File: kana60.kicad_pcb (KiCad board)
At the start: 2 copper layers, 285.5 x 115.6 mm, 151 parts, among them SW1 SW_PUSH, SW10 SW_PUSH, SW11 SW_PUSH, SW12 SW_PUSH, SW13 SW_PUSH, SW14 SW_PUSH, SW15 SW_PUSH, SW16 SW_PUSH, SW17 SW_PUSH, SW18 SW_PUSH, SW19 SW_PUSH, SW2 SW_PUSH, SW20 SW_PUSH, SW21 SW_PUSH, SW22 SW_PUSH, SW23 SW_PUSH, SW24 SW_PUSH, SW25 SW_PUSH, SW26 SW_PUSH, SW27 SW_PUSH, SW28 SW_PUSH, SW29 SW_PUSH, SW3 SW_PUSH, SW30 SW_PUSH, SW31 SW_PUSH, SW32 SW_PUSH, SW33 SW_PUSH, SW34 SW_PUSH, SW35 SW_PUSH, SW36 SW_PUSH, SW37 SW_PUSH, SW38 SW_PUSH, SW39 SW_PUSH, SW4 SW_PUSH, SW40 SW_PUSH, SW41 SW_PUSH, SW42 SW_PUSH, SW43 SW_PUSH, SW44 SW_PUSH, SW45 SW_PUSH, SW46 SW_PUSH, SW47 SW_PUSH, SW48 SW_PUSH, SW49 SW_PUSH, SW5 SW_PUSH, SW50 SW_PUSH, SW51 SW_PUSH, SW52 SW_PUSH, SW53 SW_PUSH, SW54 SW_PUSH, SW55 SW_PUSH, SW56 SW_PUSH, SW57 SW_PUSH, SW58 SW_PUSH, SW59 SW_PUSH, SW6 SW_PUSH, SW60 SW_PUSH, SW61 SW_PUSH, SW62 SW_PUSH, SW63 SW_PUSH, SW64 SW_PUSH, SW65 SW_PUSH, SW66 SW_PUSH, SW67 SW_PUSH, SW68 SW_PUSH, SW69 SW_PUSH, SW7 SW_PUSH, SW70 SW_PUSH, SW71 SW_Push, SW8 SW_PUSH, SW9 SW_PUSH, U1 ProMicro

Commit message: add GND plane
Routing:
- added copper zone on B.Cu, net GND
- added copper zone on F.Cu, net GND
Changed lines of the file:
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@@
   (segment (start 99.371685 115.062) (end 98.044 115.062) (width 0.25) (layer B.Cu) (net 89))
   (via (at 98.044 115.062) (size 0.8) (drill 0.4) (layers F.Cu B.Cu) (net 89))
+  (segment (start 72.69442 33.3877) (end 72.69442 36.77958) (width 0.25) (layer F.Cu) (net 89))
+  (segment (start 72.413988 37.060012) (end 72.413988 51.839988) (width 0.25) (layer F.Cu) (net 89))
+  (segment (start 72.69442 36.77958) (end 72.413988 37.060012) (width 0.25) (layer F.Cu) (net 89))
+  (segment (start 96.266 99.149712) (end 96.266 114.554) (width 0.25) (layer F.Cu) (net 89))
+  (segment (start 72.413988 51.839988) (end 82.042 61.468) (width 0.25) (layer F.Cu) (net 89))
+  (segment (start 82.042 61.468) (end 82.042 74.765712) (width 0.25) (layer F.Cu) (net 89))
   (segment (start 86.868 89.751712) (end 96.266 99.149712) (width 0.25) (layer F.Cu) (net 89))
+  (segment (start 86.868 79.591712) (end 86.868 89.751712) (width 0.25) (layer F.Cu) (net 89))
+  (segment (start 96.266 114.554) (end 96.774 115.062) (width 0.25) (layer F.Cu) (net 89))
+  (segment (start 96.774 115.062) (end 98.044 115.062) (width 0.25) (layer F.Cu) (net 89))
   (segment (start 82.042 74.765712) (end 86.868 79.591712) (width 0.25) (layer F.Cu) (net 89))
-  (segment (start 96.774 115.062) (end 98.044 115.062) (width 0.25) (layer F.Cu) (net 89))
-  (segment (start 72.69442 33.3877) (end 72.69442 36.77958) (width 0.25) (layer F.Cu) (net 89))
-  (segment (start 72.413988 51.839988) (end 82.042 61.468) (width 0.25) (layer F.Cu) (net 89))
-  (segment (start 72.413988 37.060012) (end 72.413988 51.839988) (width 0.25) (layer F.Cu) (net 89))
-  (segment (start 96.266 99.149712) (end 96.266 114.554) (width 0.25) (layer F.Cu) (net 89))
-  (segment (start 72.69442 36.77958) (end 72.413988 37.060012) (width 0.25) (layer F.Cu) (net 89))
-  (segment (start 96.266 114.554) (end 96.774 115.062) (width 0.25) (layer F.Cu) (net 89))
-  (segment (start 86.868 79.591712) (end 86.868 89.751712) (width 0.25) (layer F.Cu) (net 89))
-  (segment (start 82.042 61.468) (end 82.042 74.765712) (width 0.25) (layer F.Cu) (net 89))
+  (zone (net 79) (net_name GND) (layer B.Cu) (hatch edge 0.508)
+    (connect_pads (clearance 0.508))
+    (min_thickness 0.254)
+    (fill yes (arc_segments 32) (thermal_gap 0.508) (thermal_bridge_width 0.508))
+    (polygon
+      (pts
+        (xy 16.025988 19.2907) (xy 37.107988 19.2907) (xy 301.521988 19.2907) (xy 301.521988 134.8607) (xy 16.025988 134.8607)
+      )
+    )
+  )
+  (zone (net 79) (net_name GND) (layer F.Cu) (hatch edge 0.508)
+    (connect_pads (clearance 0.508))
+    (min_thickness 0.254)
+    (fill yes (arc_segments 32) (thermal_gap 0.508) (thermal_bridge_width 0.508))
+    (polygon
+      (pts
+        (xy 16.025988 19.2907) (xy 71.905988 19.2907) (xy 301.521988 19.2907) (xy 301.521988 134.8607) (xy 16.025988 134.8607)
+      )
+    )
+  )
 )

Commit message: trim anntena
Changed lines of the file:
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@@
   (segment (start 96.774 115.062) (end 98.044 115.062) (width 0.25) (layer F.Cu) (net 89))
   (segment (start 82.042 74.765712) (end 86.868 79.591712) (width 0.25) (layer F.Cu) (net 89))
+  (zone (net 79) (net_name GND) (layer F.Cu) (hatch edge 0.508)
+    (connect_pads (clearance 0.508))
+    (min_thickness 0.254)
+    (fill yes (arc_segments 32) (thermal_gap 0.508) (thermal_bridge_width 0.508))
+    (polygon
+      (pts
+        (xy 301.521988 134.8607) (xy 16.025988 134.8607) (xy 16.025988 19.2907) (xy 301.521988 19.2907)
+      )
+    )
+    (polygon
+      (pts
+        (xy 126.388988 98.9197) (xy 127.150988 99.6817) (xy 128.420988 99.6817) (xy 129.182988 100.1897) (xy 129.563988 100.8247)
+        (xy 131.087988 100.8247) (xy 129.182988 98.9197)
+      )
+    )
+    (polygon
+      (pts
+        (xy 129.690988 98.2847) (xy 131.214988 99.9357) (xy 135.405988 99.9357) (xy 135.405988 98.2847)
+      )
+    )
+    (polygon
+      (pts
+        (xy 67.460988 92.6967) (xy 72.286988 97.6497) (xy 73.302988 98.1577) (xy 73.937988 97.5227) (xy 73.556988 96.7607)
+        (xy 67.460988 90.9187)
+      )
+    )
+    (polygon
+      (pts
+        (xy 68.857988 90.7917) (xy 74.445988 96.3797) (xy 74.953988 96.6337) (xy 75.588988 96.1257) (xy 68.857988 89.6487)
+      )
+    )
+    (polygon
+      (pts
+        (xy 113.561988 81.0127) (xy 116.228988 81.0127) (xy 113.561988 78.4727)
+      )
+    )
+    (polygon
+      (pts
+        (xy 140.485988 77.3297) (xy 140.485988 78.7267) (xy 142.771988 78.7267) (xy 142.771988 77.5837) (xy 141.120988 77.5837)
+        (xy 141.120988 77.3297)
+      )
+    )
+    (polygon
+      (pts
+        (xy 37.996988 77.8377) (xy 39.520988 76.1867) (xy 37.996988 74.6627)
+      )
+    )
+    (polygon
+      (pts
+        (xy 101.877988 76.6947) (xy 101.877988 77.7107) (xy 107.592988 77.7107) (xy 107.592988 76.6947)
+      )
+    )
+    (polygon
+      (pts
+        (xy 97.940988 77.2027) (xy 100.099988 77.2027) (xy 100.099988 75.0437)
+      )
+    )
+    (polygon
+      (pts
+        (xy 141.501988 75.5517) (xy 141.501988 76.6947) (xy 145.819988 76.6947) (xy 145.819988 75.5517)
+      )
+    )
+    (polygon
+      (pts
+        (xy 102.639988 74.5357) (xy 102.639988 75.6787) (xy 107.719988 75.6787) (xy 107.719988 74.5357)
+      )
+    )
+    (polygon
+      (pts
+        (xy 142.263988 73.5197) (xy 142.263988 74.6627) (xy 148.867988 74.6627) (xy 148.867988 73.5197)
+      )
+    )
+    (polygon
+      (pts
+        (xy 103.401988 72.5037) (xy 103.401988 73.6467) (xy 110.767988 73.6467) (xy 110.767988 72.5037)
+      )
+    )
+    (polygon
+      (pts
+        (xy 97.559988 72.7577) (xy 99.337988 72.7577) (xy 99.337988 70.8527)
+      )
+    )
+    (polygon
+      (pts
+        (xy 59.713988 38.2137) (xy 59.713988 38.5947) (xy 55.649988 42.6587) (xy 55.649988 44.6907) (xy 62.126988 38.2137)
+      )
+    )
+    (polygon
+      (pts
+        (xy 29.487988 39.9917) (xy 33.805988 44.3097) (xy 33.805988 42.2777) (xy 32.027988 40.4997) (xy 32.027988 39.9917)
+      )
+    )
+    (polygon
+      (pts
+        (xy 79.779988 36.6897) (xy 79.779988 37.1977) (xy 74.953988 42.0237) (xy 74.953988 44.0557) (xy 82.319988 36.6897)
+      )
+    )
+    (polygon
+      (pts
+        (xy 39.520988 37.4517) (xy 39.520988 37.9597) (xy 35.964988 41.5157) (xy 35.964988 43.5477) (xy 42.187988 37.4517)
+      )
+    )
+    (polygon
+      (pts
+        (xy 222.146988 41.8967) (xy 222.146988 43.4207) (xy 223.416988 41.8967)
+      )
+    )
+    (polygon
+      (pts
+        (xy 56.284988 38.2137) (xy 56.284988 38.7217) (xy 54.506988 40.4997) (xy 54.506988 42.5317) (xy 58.824988 38.2137)
+      )
+    )
+    (polygon
+      (pts
+        (xy 76.604988 36.6897) (xy 76.604988 37.0707) (xy 73.937988 39.7377) (xy 73.937988 41.6427) (xy 78.890988 36.6897)
+      )
+    )
+    (polygon
+      (pts
+        (xy 32.916988 39.9917) (xy 34.440988 41.5157) (xy 34.440988 39.9917)
+      )
+    )
+    (polygon
+      (pts
+        (xy 121.562988 38.9757) (xy 122.959988 41.5157) (xy 125.372988 38.9757)
+      )
+    )
+    (polygon
+      (pts
+        (xy 36.218988 37.5787) (xy 36.218988 38.8487) (xy 35.329988 39.7377) (xy 35.329988 40.8807) (xy 38.631988 37.5787)
+      )
+    )
+    (polygon
+      (pts
+        (xy 66.444988 36.4357) (xy 70.889988 40.8807) (xy 70.889988 39.1027) (xy 68.857988 37.0707) (xy 68.857988 36.4357)
+      )
+    )
+    (polygon
+      (pts
+        (xy 49.680988 37.9597) (xy 52.220988 40.6267) (xy 52.220988 37.9597)
+      )
+    )
+    (polygon
+      (pts
+        (xy 52.982988 37.9597) (xy 52.982988 38.0867) (xy 53.363988 38.8487) (xy 53.617988 40.2457) (xy 55.522988 38.4677)
+        (xy 55.522988 37.9597)
+      )
+    )
+    (polygon
+      (pts
+        (xy 72.921988 36.8167) (xy 72.921988 39.4837) (xy 75.588988 36.8167)
+      )
+    )
+    (polygon
+      (pts
+        (xy 161.821988 39.1027) (xy 162.710988 39.1027) (xy 162.710988 34.6577) (xy 161.821988 33.6417)
+      )
+    )
+    (polygon
+      (pts
+        (xy 69.619988 36.4357) (xy 72.159988 38.9757) (xy 72.159988 36.4357)
+      )
+    )
+    (polygon
+      (pts
+        (xy 42.822988 36.1817) (xy 42.822988 38.7217) (xy 45.362988 36.1817)
+      )
+    )
+    (polygon
+      (pts
+        (xy 83.208988 34.5307) (xy 83.208988 37.1977) (xy 83.970988 37.1977) (xy 83.970988 33.8957)
+      )
+    )
+    (polygon
+      (pts
+        (xy 46.251988 34.5307) (xy 46.251988 36.6897) (xy 47.013988 36.6897) (xy 47.013988 34.0227)
+      )
+    )
+    (polygon
+      (pts
+        (xy 47.013988 24.3707) (xy 47.013988 28.4347) (xy 48.029988 27.4187) (xy 48.029988 24.3707)
+      )
+    )
+    (polygon
+      (pts
+        (xy 43.711988 25.2597) (xy 43.711988 27.0377) (xy 44.727988 27.0377) (xy 44.727988 24.2437)
+      )
+    )
+  )
   (zone (net 79) (net_name GND) (layer B.Cu) (hatch edge 0.508)
     (connect_pads (clearance 0.508))
@@
     (polygon
       (pts
-        (xy 16.025988 19.2907) (xy 37.107988 19.2907) (xy 301.521988 19.2907) (xy 301.521988 134.8607) (xy 16.025988 134.8607)
-      )
-    )
-  )
-  (zone (net 79) (net_name GND) (layer F.Cu) (hatch edge 0.508)
-    (connect_pads (clearance 0.508))
-    (min_thickness 0.254)
-    (fill yes (arc_segments 32) (thermal_gap 0.508) (thermal_bridge_width 0.508))
-    (polygon
-      (pts
-        (xy 16.025988 19.2907) (xy 71.905988 19.2907) (xy 301.521988 19.2907) (xy 301.521988 134.8607) (xy 16.025988 134.8607)
-      )
-    )
+        (xy 301.521988 134.8607) (xy 16.025988 134.8607) (xy 16.025988 19.2907) (xy 301.521988 19.2907)
+      )
+    )
+    (polygon
+      (pts
+        (xy 109.370988 76.6947) (xy 109.370988 77.7107) (xy 144.295988 77.7107) (xy 144.295988 76.6947)
+      )
+    )

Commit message: change revision to 1.1 from 1.0
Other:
- board text added: "rev.1.1"
- board text removed: "rev.1.0"
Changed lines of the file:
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@@
   (title_block
     (title kana60)
-    (date 2019-07-02)
-    (rev rev.1)
+    (date 2019-10-13)
+    (rev rev.1.1)
     (comment 1 https://github.com/sasaplus1/kana60)
     (comment 2 "designed by sasa+1")
@@
   (gr_line (start 301.521988 133.0827) (end 301.521988 21.0687) (layer Edge.Cuts) (width 0.2))
   (gr_line (start 17.803988 19.2907) (end 299.743988 19.2907) (layer Edge.Cuts) (width 0.2))
-  (gr_text rev.1.0 (at 226.314 76.962) (layer B.SilkS)
+  (gr_text rev.1.1 (at 226.314 76.962) (layer B.SilkS)
     (effects (font (size 1 1) (thickness 0.15)) (justify mirror))
   )

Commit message: update captions
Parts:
- moved G*** 0.75 mm to (243.3, 75.2)
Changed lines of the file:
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@@
   )
   (module kana60:kana60-title (layer B.Cu)
-    (at 243.332 74.422 180)
+    (at 243.332 75.1707 180)
     (fp_text reference G*** (at 0 0) (layer B.SilkS) hide
       (effects (font (size 1.524 1.524) (thickness 0.3)) (justify mirror))
@@
   (gr_line (start 301.521988 133.0827) (end 301.521988 21.0687) (layer Edge.Cuts) (width 0.2))
   (gr_line (start 17.803988 19.2907) (end 299.743988 19.2907) (layer Edge.Cuts) (width 0.2))
-  (gr_text rev.1.1 (at 226.314 76.962) (layer B.SilkS)
-    (effects (font (size 1 1) (thickness 0.15)) (justify mirror))
+  (gr_text rev.1.1 (at 225.067988 77.7107) (layer B.SilkS)
+    (effects (font (size 1.2 1.2) (thickness 0.15)) (justify mirror))
   )
-  (gr_text "designed by sasa+1" (at 78.001988 75.1707) (layer B.SilkS)
-    (effects (font (size 1 1) (thickness 0.15)) (justify mirror))
+  (gr_text "designed by sasa+1" (at 78.001988 76.1867) (layer B.SilkS)
+    (effects (font (size 1.2 1.2) (thickness 0.15)) (justify mirror))
   )
   (gr_line (start 285.11475 56.27635) (end 285.11475 42.27675) (layer Dwgs.User) (width 0.2))

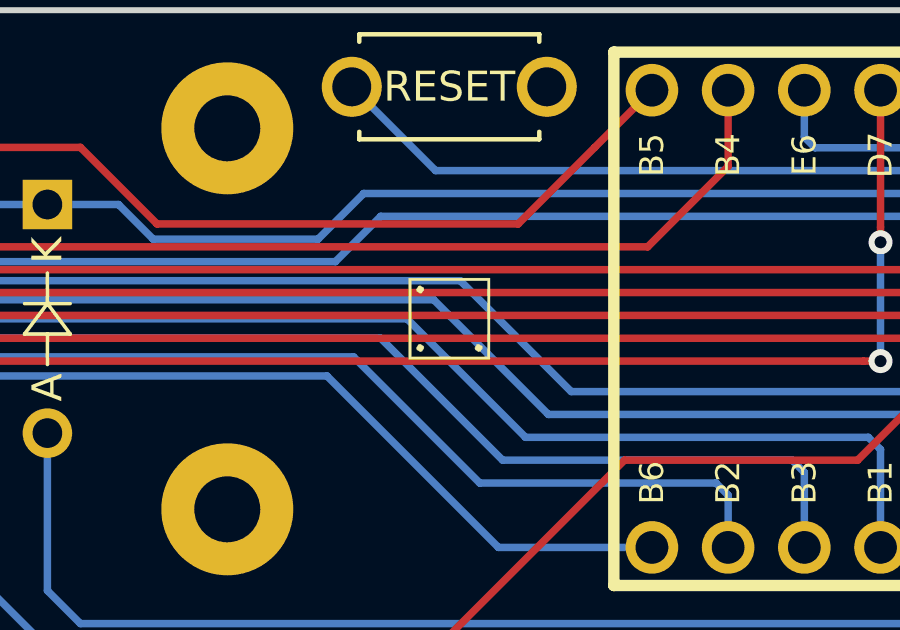
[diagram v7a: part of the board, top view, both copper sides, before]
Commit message: update icon
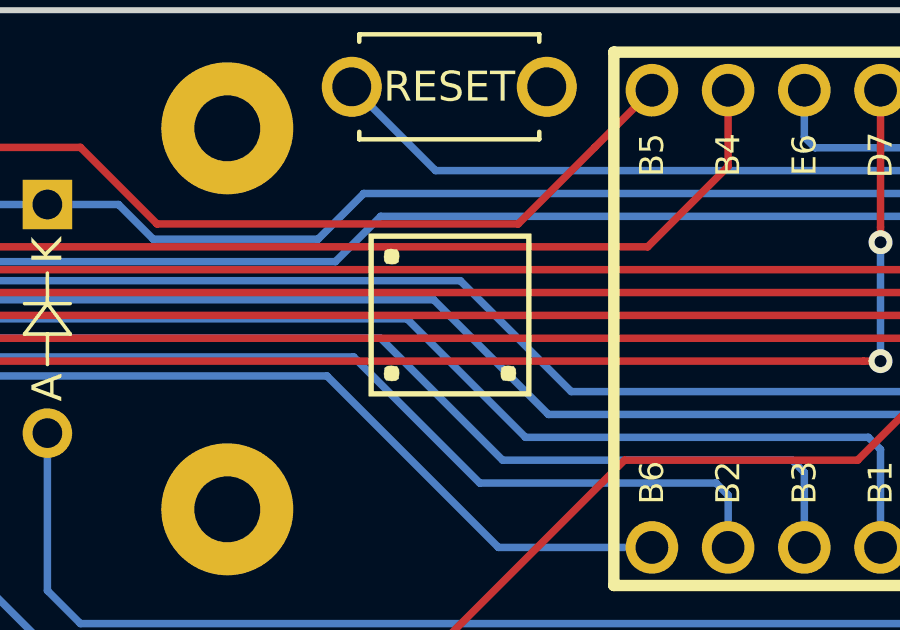
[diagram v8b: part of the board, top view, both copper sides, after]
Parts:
- removed the G*** at (67.6, 75.2)
- removed the G*** at (260.6, 29.6)
- added G***: LOGO, kicad-footprints:sasaplus1-icon-64, F.Cu at (260.6, 29.5)
- added G***: LOGO, kicad-footprints:sasaplus1-icon-48, B.Cu at (64.5, 76.2)
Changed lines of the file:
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@@
     (add_net GND)
+  )
+  (module kicad-footprints:sasaplus1-icon-64 (layer F.Cu)
+    (at 260.627988 29.4507)
+    (fp_text reference G*** (at 0 0) (layer F.SilkS) hide
+      (effects (font (size 1.524 1.524) (thickness 0.3)))
+    )
+    (fp_text value LOGO (at 0 0) (layer F.SilkS) hide
+      (effects (font (size 1.524 1.524) (thickness 0.3)))
+    )
+    (fp_poly (pts (xy -1.767425 -2.180354) (xy -1.701115 -2.081394) (xy -1.693333 -1.947333) (xy -1.714313 -1.767425)
+      (xy -1.813273 -1.701115) (xy -1.947333 -1.693333) (xy -2.127242 -1.714313) (xy -2.193552 -1.813273)
+      (xy -2.201333 -1.947333) (xy -2.180354 -2.127242) (xy -2.081394 -2.193552) (xy -1.947333 -2.201333)
+      (xy -1.767425 -2.180354)) (layer F.SilkS) (width 0.01))
+    (fp_poly (pts (xy 2.127241 1.714312) (xy 2.193552 1.813273) (xy 2.201333 1.947333) (xy 2.180354 2.127241)
+      (xy 2.081393 2.193552) (xy 1.947333 2.201333) (xy 1.767425 2.180354) (xy 1.701115 2.081393)
+      (xy 1.693333 1.947333) (xy 1.714312 1.767425) (xy 1.813273 1.701115) (xy 1.947333 1.693333)
+      (xy 2.127241 1.714312)) (layer F.SilkS) (width 0.01))
+    (fp_poly (pts (xy -1.767425 1.714312) (xy -1.701115 1.813273) (xy -1.693333 1.947333) (xy -1.714313 2.127241)
+      (xy -1.813273 2.193552) (xy -1.947333 2.201333) (xy -2.127242 2.180354) (xy -2.193552 2.081393)
+      (xy -2.201333 1.947333) (xy -2.180354 1.767425) (xy -2.081394 1.701115) (xy -1.947333 1.693333)
+      (xy -1.767425 1.714312)) (layer F.SilkS) (width 0.01))
+    (fp_poly (pts (xy 2.709333 2.709333) (xy -2.709333 2.709333) (xy -2.709333 -2.54) (xy -2.54 -2.54)
+      (xy -2.54 2.54) (xy 2.54 2.54) (xy 2.54 -2.54) (xy -2.54 -2.54)
+      (xy -2.709333 -2.54) (xy -2.709333 -2.709333) (xy 2.709333 -2.709333) (xy 2.709333 2.709333)) (layer F.SilkS) (width 0.01))
+  )
+  (module kicad-footprints:sasaplus1-icon-48 (layer B.Cu)
+    (at 64.539988 76.1867 180)
+    (fp_text reference G*** (at 0 0) (layer B.SilkS) hide
+      (effects (font (size 1.524 1.524) (thickness 0.3)) (justify mirror))
+    )
+    (fp_text value LOGO (at 0 0) (layer B.SilkS) hide
+      (effects (font (size 1.524 1.524) (thickness 0.3)) (justify mirror))
+    )
+    (fp_poly (pts (xy -1.235879 1.573698) (xy -1.186228 1.436007) (xy -1.185334 1.397) (xy -1.220303 1.235879)
+      (xy -1.357994 1.186228) (xy -1.397 1.185334) (xy -1.558122 1.220303) (xy -1.607773 1.357994)
+      (xy -1.608667 1.397) (xy -1.573698 1.558122) (xy -1.436007 1.607773) (xy -1.397 1.608667)
+      (xy -1.235879 1.573698)) (layer B.SilkS) (width 0.01))
+    (fp_poly (pts (xy 1.558121 -1.220302) (xy 1.607772 -1.357993) (xy 1.608666 -1.397) (xy 1.573697 -1.558121)
+      (xy 1.436006 -1.607772) (xy 1.397 -1.608666) (xy 1.235878 -1.573697) (xy 1.186227 -1.436006)
+      (xy 1.185333 -1.397) (xy 1.220302 -1.235878) (xy 1.357993 -1.186227) (xy 1.397 -1.185333)
+      (xy 1.558121 -1.220302)) (layer B.SilkS) (width 0.01))
+    (fp_poly (pts (xy -1.235879 -1.220302) (xy -1.186228 -1.357993) (xy -1.185334 -1.397) (xy -1.220303 -1.558121)
+      (xy -1.357994 -1.607772) (xy -1.397 -1.608666) (xy -1.558122 -1.573697) (xy -1.607773 -1.436006)
+      (xy -1.608667 -1.397) (xy -1.573698 -1.235878) (xy -1.436007 -1.186227) (xy -1.397 -1.185333)
+      (xy -1.235879 -1.220302)) (layer B.SilkS) (width 0.01))
+    (fp_poly (pts (xy 2.032 -2.032) (xy -2.032 -2.032) (xy -2.032 1.862667) (xy -1.862667 1.862667)
+      (xy -1.862667 -1.862666) (xy 1.862666 -1.862666) (xy 1.862666 1.862667) (xy -1.862667 1.862667)
+      (xy -2.032 1.862667) (xy -2.032 2.032) (xy 2.032 2.032) (xy 2.032 -2.032)) (layer B.SilkS) (width 0.01))
   )
   (module Keebio-Parts:Hybrid_PCB_125H (layer F.Cu)
@@
       (xy -7.044052 1.138264)) (layer B.SilkS) (width 0.01))
   )
-  (module kicad-footprints:sasaplus1-icon (layer B.Cu)
-    (at 67.564 75.184 180)
-    (fp_text reference G*** (at 0 0) (layer B.SilkS) hide
-      (effects (font (size 1.524 1.524) (thickness 0.3)) (justify mirror))
-    )
-    (fp_text value LOGO (at 0.75 0) (layer B.SilkS) hide
-      (effects (font (size 1.524 1.524) (thickness 0.3)) (justify mirror))
-    )
-    (fp_poly (pts (xy -0.861418 1.032894) (xy -0.846666 0.973666) (xy -0.914439 0.861418) (xy -0.973666 0.846666)
-      (xy -1.085915 0.914439) (xy -1.100666 0.973666) (xy -1.032894 1.085915) (xy -0.973666 1.100666)
-      (xy -0.861418 1.032894)) (layer B.SilkS) (width 0.01))
-    (fp_poly (pts (xy 1.085915 -0.91444) (xy 1.100667 -0.973667) (xy 1.032894 -1.085915) (xy 0.973667 -1.100667)
-      (xy 0.861418 -1.032894) (xy 0.846667 -0.973667) (xy 0.91444 -0.861418) (xy 0.973667 -0.846667)
-      (xy 1.085915 -0.91444)) (layer B.SilkS) (width 0.01))
-    (fp_poly (pts (xy -0.861418 -0.91444) (xy -0.846666 -0.973667) (xy -0.914439 -1.085915) (xy -0.973666 -1.100667)
-      (xy -1.085915 -1.032894) (xy -1.100666 -0.973667) (xy -1.032894 -0.861418) (xy -0.973666 -0.846667)
-      (xy -0.861418 -0.91444)) (layer B.SilkS) (width 0.01))
-    (fp_poly (pts (xy 1.354667 -1.354667) (xy -1.354666 -1.354667) (xy -1.354666 1.27) (xy -1.27 1.27)
-      (xy -1.27 -1.27) (xy 1.27 -1.27) (xy 1.27 1.27) (xy -1.27 1.27)
-      (xy -1.354666 1.27) (xy -1.354666 1.354666) (xy 1.354667 1.354666) (xy 1.354667 -1.354667)) (layer B.SilkS) (width 0.01))
-  )
-  (module kicad-footprints:sasaplus1-icon (layer F.Cu)
-    (at 260.607988 29.5747)
-    (fp_text reference G*** (at 0 0) (layer F.SilkS) hide
-      (effects (font (size 1.524 1.524) (thickness 0.3)))
-    )
-    (fp_text value LOGO (at 0.75 0) (layer F.SilkS) hide
-      (effects (font (size 1.524 1.524) (thickness 0.3)))
-    )
-    (fp_poly (pts (xy 1.354667 1.354667) (xy -1.354666 1.354667) (xy -1.354666 -1.27) (xy -1.27 -1.27)
-      (xy -1.27 1.27) (xy 1.27 1.27) (xy 1.27 -1.27) (xy -1.27 -1.27)
-      (xy -1.354666 -1.27) (xy -1.354666 -1.354666) (xy 1.354667 -1.354666) (xy 1.354667 1.354667)) (layer F.SilkS) (width 0.01))
-    (fp_poly (pts (xy -0.861418 0.91444) (xy -0.846666 0.973667) (xy -0.914439 1.085915) (xy -0.973666 1.100667)
-      (xy -1.085915 1.032894) (xy -1.100666 0.973667) (xy -1.032894 0.861418) (xy -0.973666 0.846667)
-      (xy -0.861418 0.91444)) (layer F.SilkS) (width 0.01))
-    (fp_poly (pts (xy 1.085915 0.91444) (xy 1.100667 0.973667) (xy 1.032894 1.085915) (xy 0.973667 1.100667)
-      (xy 0.861418 1.032894) (xy 0.846667 0.973667) (xy 0.91444 0.861418) (xy 0.973667 0.846667)
-      (xy 1.085915 0.91444)) (layer F.SilkS) (width 0.01))
-    (fp_poly (pts (xy -0.861418 -1.032894) (xy -0.846666 -0.973666) (xy -0.914439 -0.861418) (xy -0.973666 -0.846666)
-      (xy -1.085915 -0.914439) (xy -1.100666 -0.973666) (xy -1.032894 -1.085915) (xy -0.973666 -1.100666)
-      (xy -0.861418 -1.032894)) (layer F.SilkS) (width 0.01))
-  )
   (module Keebio-Parts:Hybrid_PCB_100H (layer F.Cu)
